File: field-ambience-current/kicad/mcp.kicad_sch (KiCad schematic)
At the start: 45 parts, among them SW1 Cell 1 (2u Choc V2 Hot-Swap), SW10 Modifier CLEAR (12x12x7.3 SMD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, SW2 Cell 2 (2u Choc V2 Hot-Swap), SW3 Cell 3 (2u Choc V2 Hot-Swap), SW4 Cell 4 (2u Choc V2 Hot-Swap), SW5 Cell 5 (2u Choc V2 Hot-Swap), SW6 Modifier SHIFT (12x12x7.3 SMD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, SW7 Modifier HOLD (12x12x7.3 SMD-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, SW8 Modifier DRONE (12x12x7.3 SMD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, SW9 Modifier GENERATE (12x12x7.3 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, U2 MCP23017-E/SS (I/O-Expander), U6 PCA9685PW (16-Ch I²C PWM LED-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

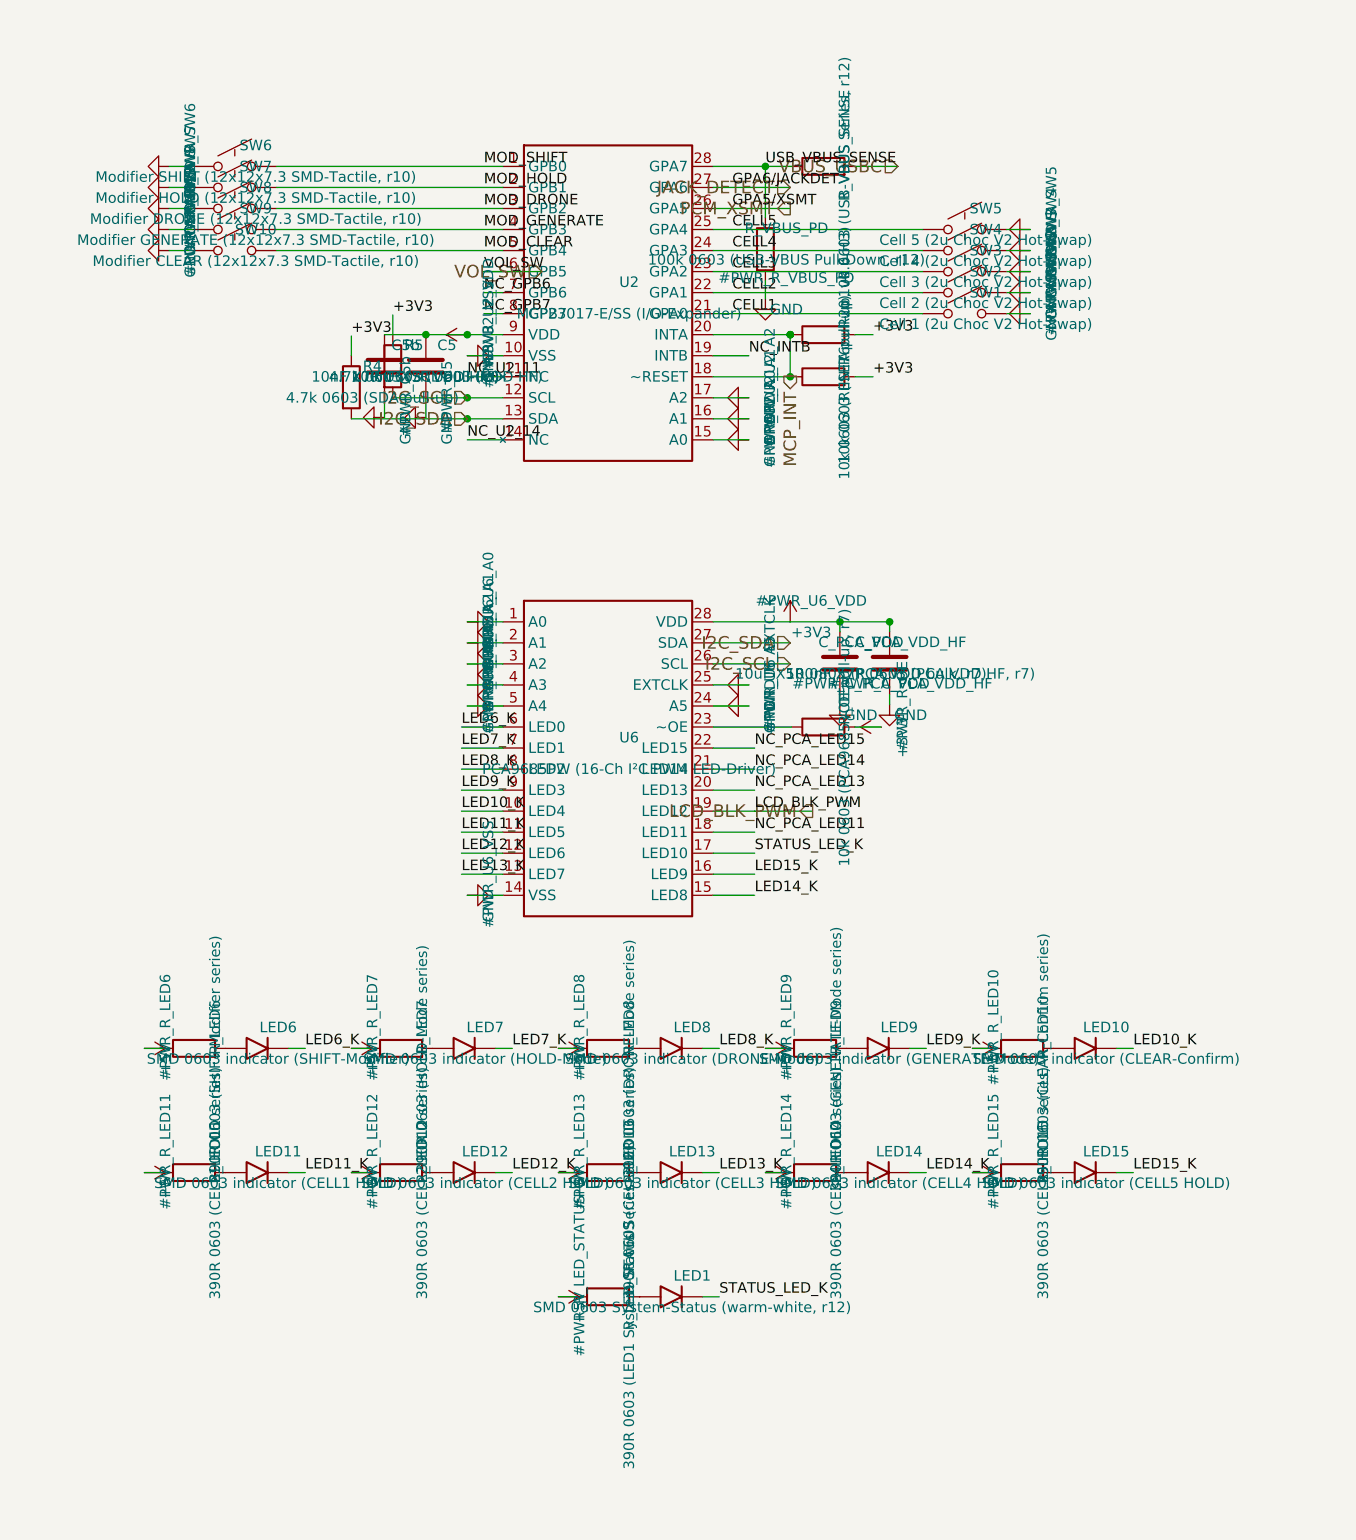
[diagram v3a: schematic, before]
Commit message: pcb(r18.9): Schematic-Implementation IMG_9713 — Cell-FSR-ADC + 15-LED-Topologie
Implementiert die r18.8-Design-Entscheidungen (ADR-0006/0008) im Generator.

=== Cell-Velocity (ADR-0006) ===

- stm32h743_sheet: 5 ADC-Netze CELL1..5_SENSE an PC0(15)/PC1(16)/
  PA4(28)/PB0(34)/PB1(35) — vorher no_connect, alle Standard-ADC12.
  FSR-Interface pro Cell: J_CELLn 2-Pin von +3V3, 10k Teiler-Bottom,
  10nF S/H-Filter, Knoten -> ADC-Pin
- ADR-0006-KORREKTUR: Erstfassung nannte PA0/PA1/PA2/PA6 als frei —
  FALSCH (PA0/PA1=TIM2-Encoder, PA6=LCD_CS). Gegen verifizierte
  Pin-Tabelle ersetzt, transparent im ADR vermerkt
- mcp_sheet: SW1-5 Kailh-Choc-Hotswap komplett raus, GPA0-4 -> NC
  (Rev-B-Reserve). BOM: -5 Hotswap-Sockets, -5 Stabilizer;
  +5 J_CELL, +5 R10k, +5 C10nF, +5 FSR (separat beschafft)
- SPEC §5.6a NEU: Cell-Sense-Pin-Tabelle

=== LED-Topologie (ADR-0008) ===

- led_array 10 -> 15 LEDs, farbcodiert:
  LED6 gruen (Shift), LED7 gelb (Hold), LED8-10 weiss (Drone/Gen/Clear),
  LED11Y/G..LED15Y/G = 5x2 Cell-LEDs (XOR gelb/gruen)
- PCA-Kanaele 0-14 = LEDs, Kanal 15 = LCD_BLK_PWM (war ch12).
  16/16 exakt — kein Reserve-Kanal
- LED1+R_LED_STATUS (r12 PCA-ch10-Status) entfernt — Heartbeat ist
  LED_HB an MCU-PD8 seit r18.5. ch10 jetzt LED13G
- Gelb/Gruen-MPNs XL-1608UYC/UGC-04 als Kandidaten (TBD-VERIFY-Stock)
- 390R einheitlich: gelb/gruen ~7.4mA, weiss ~5.1mA — beide im
  PCA-Sink-Budget, Matching per Firmware-PWM

=== Validierung ===

paren 8/8 - 100/100 STM32-Pins (5 Cell-Pins WIRE statt no_connect) -
mcp: 15 LEDs, 0 STATUS/NC_PCA/Choc-Reste, NC_GPA0-4 da, BLK-hier
intakt - Crossref 7/7 PASS

Scores: Schematic 8->9, LED-Logik 9->10, Cell-Mechanik 3->5.
KEIN .kicad_pcb — Gate-Status unveraendert.

https://claude.ai/code/session_01K5kLTFpDCCoYwx2dq6RkAv
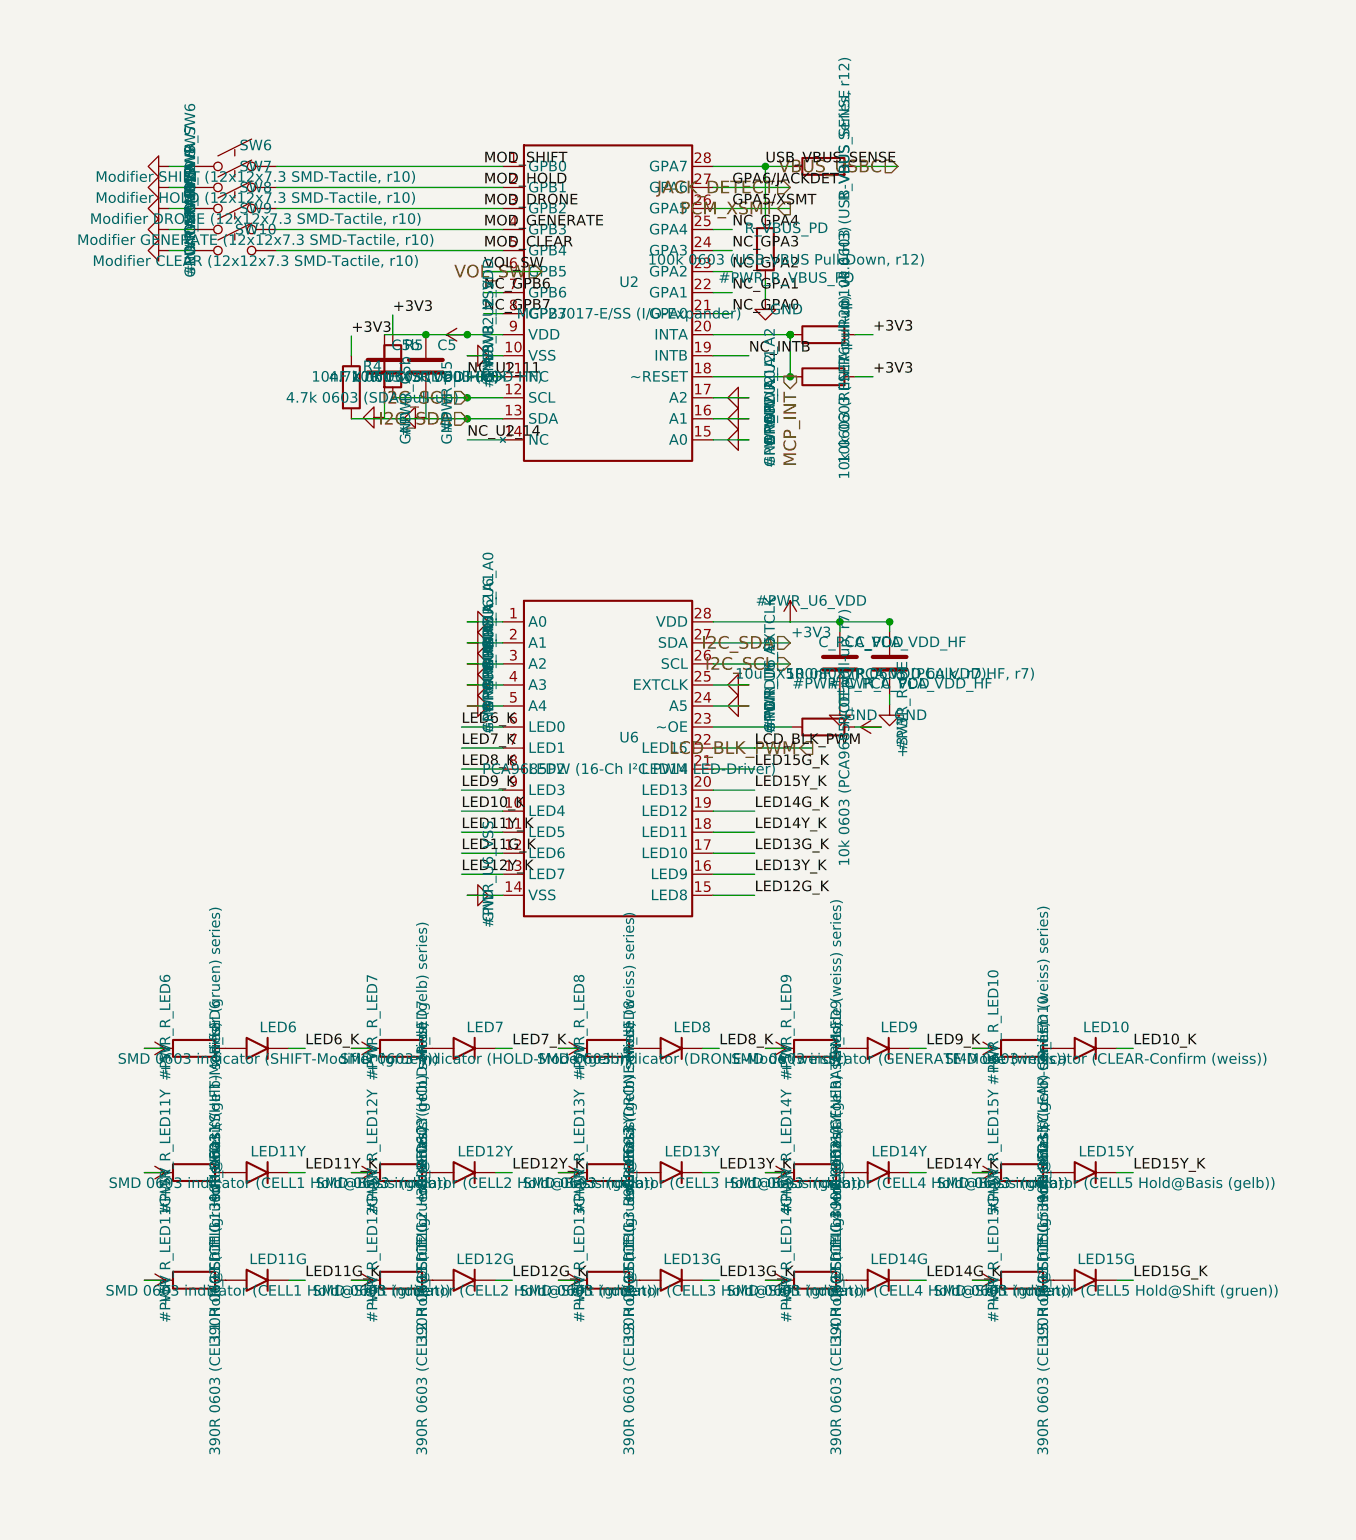
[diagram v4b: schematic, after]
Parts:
- removed LED1: SMD 0603 System-Status (warm-white, r12), LED_SMD:LED_0603_1608Metric, symbol Device:LED
- removed LED11: SMD 0603 indicator (CELL1 HOLD), LED_SMD:LED_0603_1608Metric, symbol Device:LED
- removed LED12: SMD 0603 indicator (CELL2 HOLD), LED_SMD:LED_0603_1608Metric, symbol Device:LED
- removed LED13: SMD 0603 indicator (CELL3 HOLD), LED_SMD:LED_0603_1608Metric, symbol Device:LED
- removed LED14: SMD 0603 indicator (CELL4 HOLD), LED_SMD:LED_0603_1608Metric, symbol Device:LED
- removed LED15: SMD 0603 indicator (CELL5 HOLD), LED_SMD:LED_0603_1608Metric, symbol Device:LED
- removed R_LED11: 390R 0603 (CELL1 HOLD series), Resistor_SMD:R_0603_1608Metric, symbol Device:R
- removed R_LED12: 390R 0603 (CELL2 HOLD series), Resistor_SMD:R_0603_1608Metric, symbol Device:R
- removed R_LED13: 390R 0603 (CELL3 HOLD series), Resistor_SMD:R_0603_1608Metric, symbol Device:R
- removed R_LED14: 390R 0603 (CELL4 HOLD series), Resistor_SMD:R_0603_1608Metric, symbol Device:R
- removed R_LED15: 390R 0603 (CELL5 HOLD series), Resistor_SMD:R_0603_1608Metric, symbol Device:R
- removed R_LED_STATUS: 390R 0603 (LED1 System-Status Series, r12), Resistor_SMD:R_0603_1608Metric, symbol Device:R
- removed SW1: Cell 1 (2u Choc V2 Hot-Swap), Switch_Keyboard_Hotswap_Kailh:SW_Hotswap_Kailh_Choc_V1V2_2.00u, symbol Switch:SW_Push
- removed SW2: Cell 2 (2u Choc V2 Hot-Swap), Switch_Keyboard_Hotswap_Kailh:SW_Hotswap_Kailh_Choc_V1V2_2.00u, symbol Switch:SW_Push
- removed SW3: Cell 3 (2u Choc V2 Hot-Swap), Switch_Keyboard_Hotswap_Kailh:SW_Hotswap_Kailh_Choc_V1V2_2.00u, symbol Switch:SW_Push
- removed SW4: Cell 4 (2u Choc V2 Hot-Swap), Switch_Keyboard_Hotswap_Kailh:SW_Hotswap_Kailh_Choc_V1V2_2.00u, symbol Switch:SW_Push
- removed SW5: Cell 5 (2u Choc V2 Hot-Swap), Switch_Keyboard_Hotswap_Kailh:SW_Hotswap_Kailh_Choc_V1V2_2.00u, symbol Switch:SW_Push
- added LED11G: SMD 0603 indicator (CELL1 Hold@Shift (gruen)), LED_SMD:LED_0603_1608Metric, symbol Device:LED
- added LED11Y: SMD 0603 indicator (CELL1 Hold@Basis (gelb)), LED_SMD:LED_0603_1608Metric, symbol Device:LED
- added LED12G: SMD 0603 indicator (CELL2 Hold@Shift (gruen)), LED_SMD:LED_0603_1608Metric, symbol Device:LED
- added LED12Y: SMD 0603 indicator (CELL2 Hold@Basis (gelb)), LED_SMD:LED_0603_1608Metric, symbol Device:LED
- added LED13G: SMD 0603 indicator (CELL3 Hold@Shift (gruen)), LED_SMD:LED_0603_1608Metric, symbol Device:LED
- added LED13Y: SMD 0603 indicator (CELL3 Hold@Basis (gelb)), LED_SMD:LED_0603_1608Metric, symbol Device:LED
- added LED14G: SMD 0603 indicator (CELL4 Hold@Shift (gruen)), LED_SMD:LED_0603_1608Metric, symbol Device:LED
- added LED14Y: SMD 0603 indicator (CELL4 Hold@Basis (gelb)), LED_SMD:LED_0603_1608Metric, symbol Device:LED
- added LED15G: SMD 0603 indicator (CELL5 Hold@Shift (gruen)), LED_SMD:LED_0603_1608Metric, symbol Device:LED
- added LED15Y: SMD 0603 indicator (CELL5 Hold@Basis (gelb)), LED_SMD:LED_0603_1608Metric, symbol Device:LED
- added R_LED11G: 390R 0603 (CELL1 Hold@Shift (gruen) series), Resistor_SMD:R_0603_1608Metric, symbol Device:R
- added R_LED11Y: 390R 0603 (CELL1 Hold@Basis (gelb) series), Resistor_SMD:R_0603_1608Metric, symbol Device:R
- added R_LED12G: 390R 0603 (CELL2 Hold@Shift (gruen) series), Resistor_SMD:R_0603_1608Metric, symbol Device:R
- added R_LED12Y: 390R 0603 (CELL2 Hold@Basis (gelb) series), Resistor_SMD:R_0603_1608Metric, symbol Device:R
- added R_LED13G: 390R 0603 (CELL3 Hold@Shift (gruen) series), Resistor_SMD:R_0603_1608Metric, symbol Device:R
- added R_LED13Y: 390R 0603 (CELL3 Hold@Basis (gelb) series), Resistor_SMD:R_0603_1608Metric, symbol Device:R
- added R_LED14G: 390R 0603 (CELL4 Hold@Shift (gruen) series), Resistor_SMD:R_0603_1608Metric, symbol Device:R
- added R_LED14Y: 390R 0603 (CELL4 Hold@Basis (gelb) series), Resistor_SMD:R_0603_1608Metric, symbol Device:R
- added R_LED15G: 390R 0603 (CELL5 Hold@Shift (gruen) series), Resistor_SMD:R_0603_1608Metric, symbol Device:R
- added R_LED15Y: 390R 0603 (CELL5 Hold@Basis (gelb) series), Resistor_SMD:R_0603_1608Metric, symbol Device:R
- LED10: value SMD 0603 indicator (CLEAR-Confirm) -> SMD 0603 indicator (CLEAR-Confirm (weiss)); MPN XL-1608UWC-04 (warm-white 0603, Extended) -> XL-1608UWC-04 (warm-white 0603)
- LED6: value SMD 0603 indicator (SHIFT-Modifier) -> SMD 0603 indicator (SHIFT-Modifier (gruen)); LCSC C965808 -> TBD-VERIFY (JLC-Stock gruen 0603); MPN XL-1608UWC-04 (warm-white 0603, Extended) -> XL-1608UGC-04 (green 0603, XINGLIGHT-Serie)
- LED7: value SMD 0603 indicator (HOLD-Mode) -> SMD 0603 indicator (HOLD-Mode (gelb)); LCSC C965808 -> TBD-VERIFY (JLC-Stock gelb 0603); MPN XL-1608UWC-04 (warm-white 0603, Extended) -> XL-1608UYC-04 (yellow 0603, XINGLIGHT-Serie)
- LED8: value SMD 0603 indicator (DRONE-Mode) -> SMD 0603 indicator (DRONE-Mode (weiss)); MPN XL-1608UWC-04 (warm-white 0603, Extended) -> XL-1608UWC-04 (warm-white 0603)
- LED9: value SMD 0603 indicator (GENERATE-Mode) -> SMD 0603 indicator (GENERATE-Mode (weiss)); MPN XL-1608UWC-04 (warm-white 0603, Extended) -> XL-1608UWC-04 (warm-white 0603)
- R_LED10: value 390R 0603 (CLEAR-Confirm series) -> 390R 0603 (CLEAR-Confirm (weiss) series)
- R_LED6: value 390R 0603 (SHIFT-Modifier series) -> 390R 0603 (SHIFT-Modifier (gruen) series)
- R_LED7: value 390R 0603 (HOLD-Mode series) -> 390R 0603 (HOLD-Mode (gelb) series)
- R_LED8: value 390R 0603 (DRONE-Mode series) -> 390R 0603 (DRONE-Mode (weiss) series)
- R_LED9: value 390R 0603 (GENERATE-Mode series) -> 390R 0603 (GENERATE-Mode (weiss) series)
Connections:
- net NC_PCA_LED15 is gone; now on net LCD_BLK_PWM: U6.22 (LED15)
- net +5V: now also R_LED11G.1, R_LED11Y.1, R_LED12G.1, R_LED12Y.1, R_LED13G.1, R_LED13Y.1, R_LED14G.1, R_LED14Y.1, R_LED15G.1, R_LED15Y.1
- net LCD_BLK_PWM: no longer U6.19 (LED12)
- net CELL1 renamed NC_GPA0
- net CELL2 renamed NC_GPA1
- net CELL3 renamed NC_GPA2
- net CELL4 renamed NC_GPA3
- net CELL5 renamed NC_GPA4
- net LED11_K renamed LED11Y_K
- net LED11Y_K: now also LED11Y.1 (K)
- net LED12_K renamed LED11G_K
- net LED11G_K: now also LED11G.1 (K)
- net LED13_K renamed LED12Y_K
- net LED12Y_K: now also LED12Y.1 (K)
- net LED14_K renamed LED12G_K
- net LED12G_K: now also LED12G.1 (K)
- net LED15_K renamed LED13Y_K
- net LED13Y_K: now also LED13Y.1 (K)
- net NC_PCA_LED11 renamed LED14Y_K
- net LED14Y_K: now also LED14Y.1 (K)
- net NC_PCA_LED13 renamed LED15Y_K
- net LED15Y_K: now also LED15Y.1 (K)
- net NC_PCA_LED14 renamed LED15G_K
- net LED15G_K: now also LED15G.1 (K)
- net STATUS_LED_K renamed LED13G_K
- net LED13G_K: now also LED13G.1 (K)
- new net: LED12G.2 (A), R_LED12G.2
- new net: LED11G.2 (A), R_LED11G.2
- new net: LED11Y.2 (A), R_LED11Y.2
- new net: LED13Y.2 (A), R_LED13Y.2
- new net: LED14G.2 (A), R_LED14G.2
- new net: LED13G.2 (A), R_LED13G.2
- new net: LED15G.2 (A), R_LED15G.2
- new net: LED14Y.2 (A), R_LED14Y.2
- new net: LED15Y.2 (A), R_LED15Y.2
- new net: LED12Y.2 (A), R_LED12Y.2
- new net LED14G_K: LED14G.1 (K), U6.19 (LED12)
